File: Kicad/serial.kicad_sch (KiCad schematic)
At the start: 9 parts, among them J801 Conn_02x05, J802 DB9_Male_MountingHoles, U801 ST3232CDR

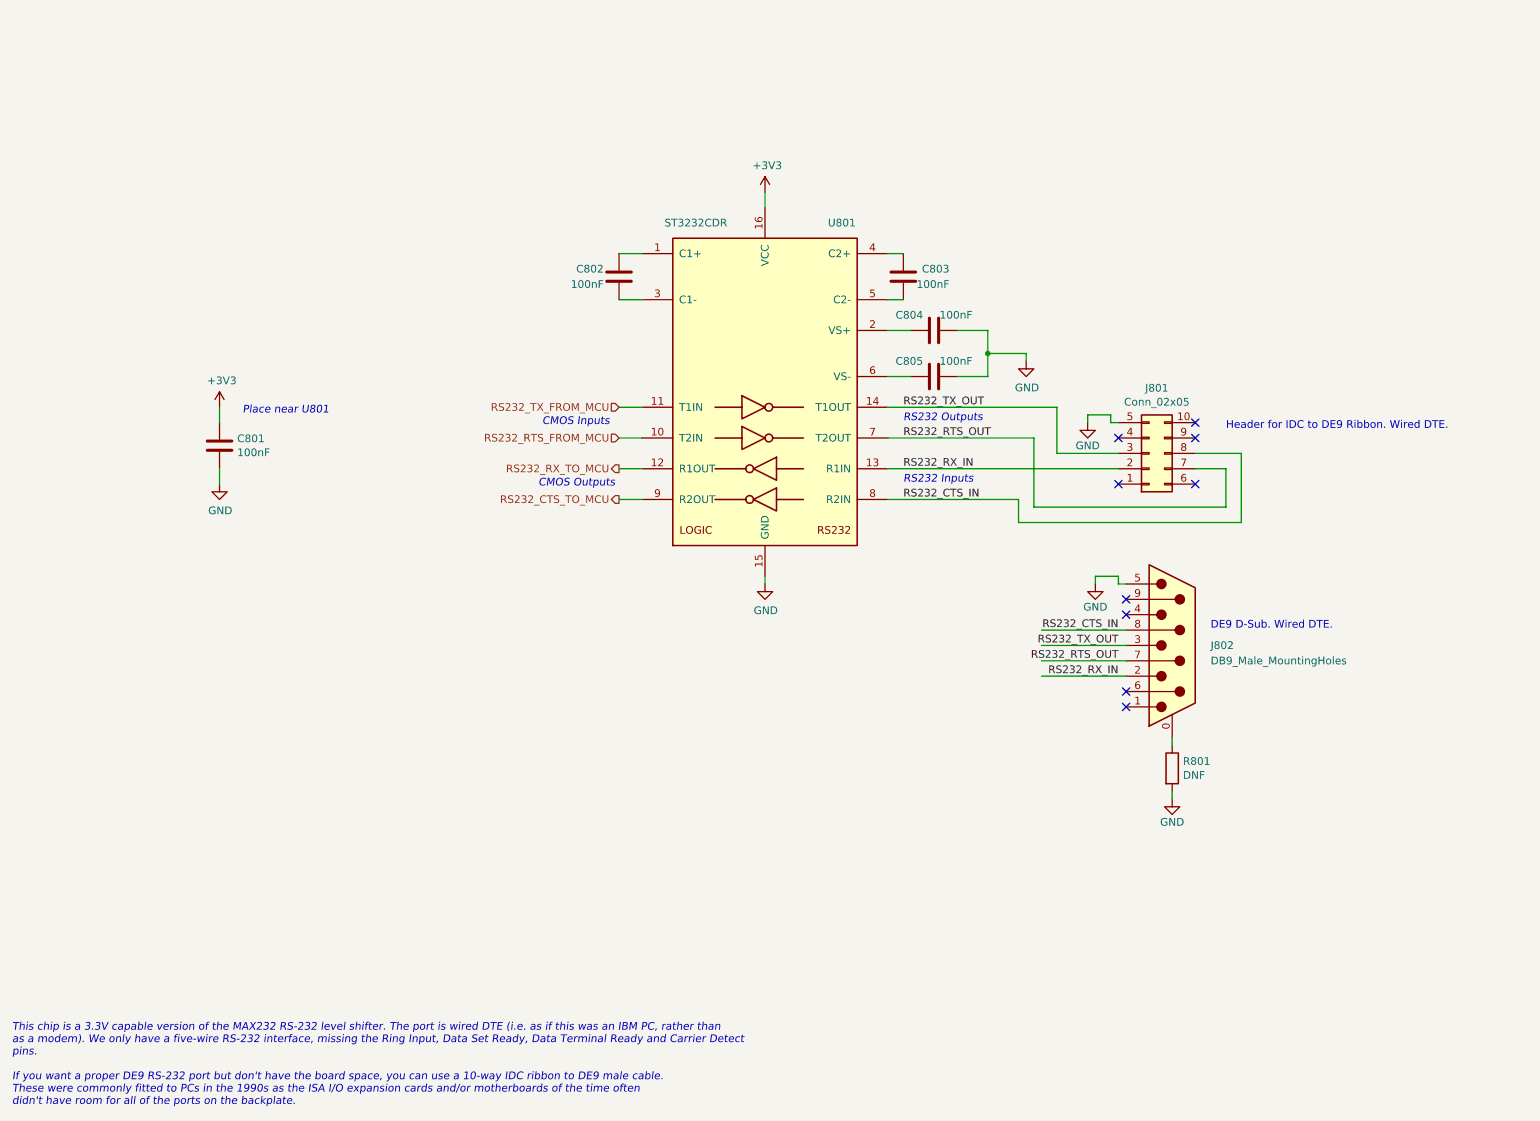
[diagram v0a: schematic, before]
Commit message: Update schematic files to Kicad 6.
Had to fix some symbols which didn't have perfect matches in K6.
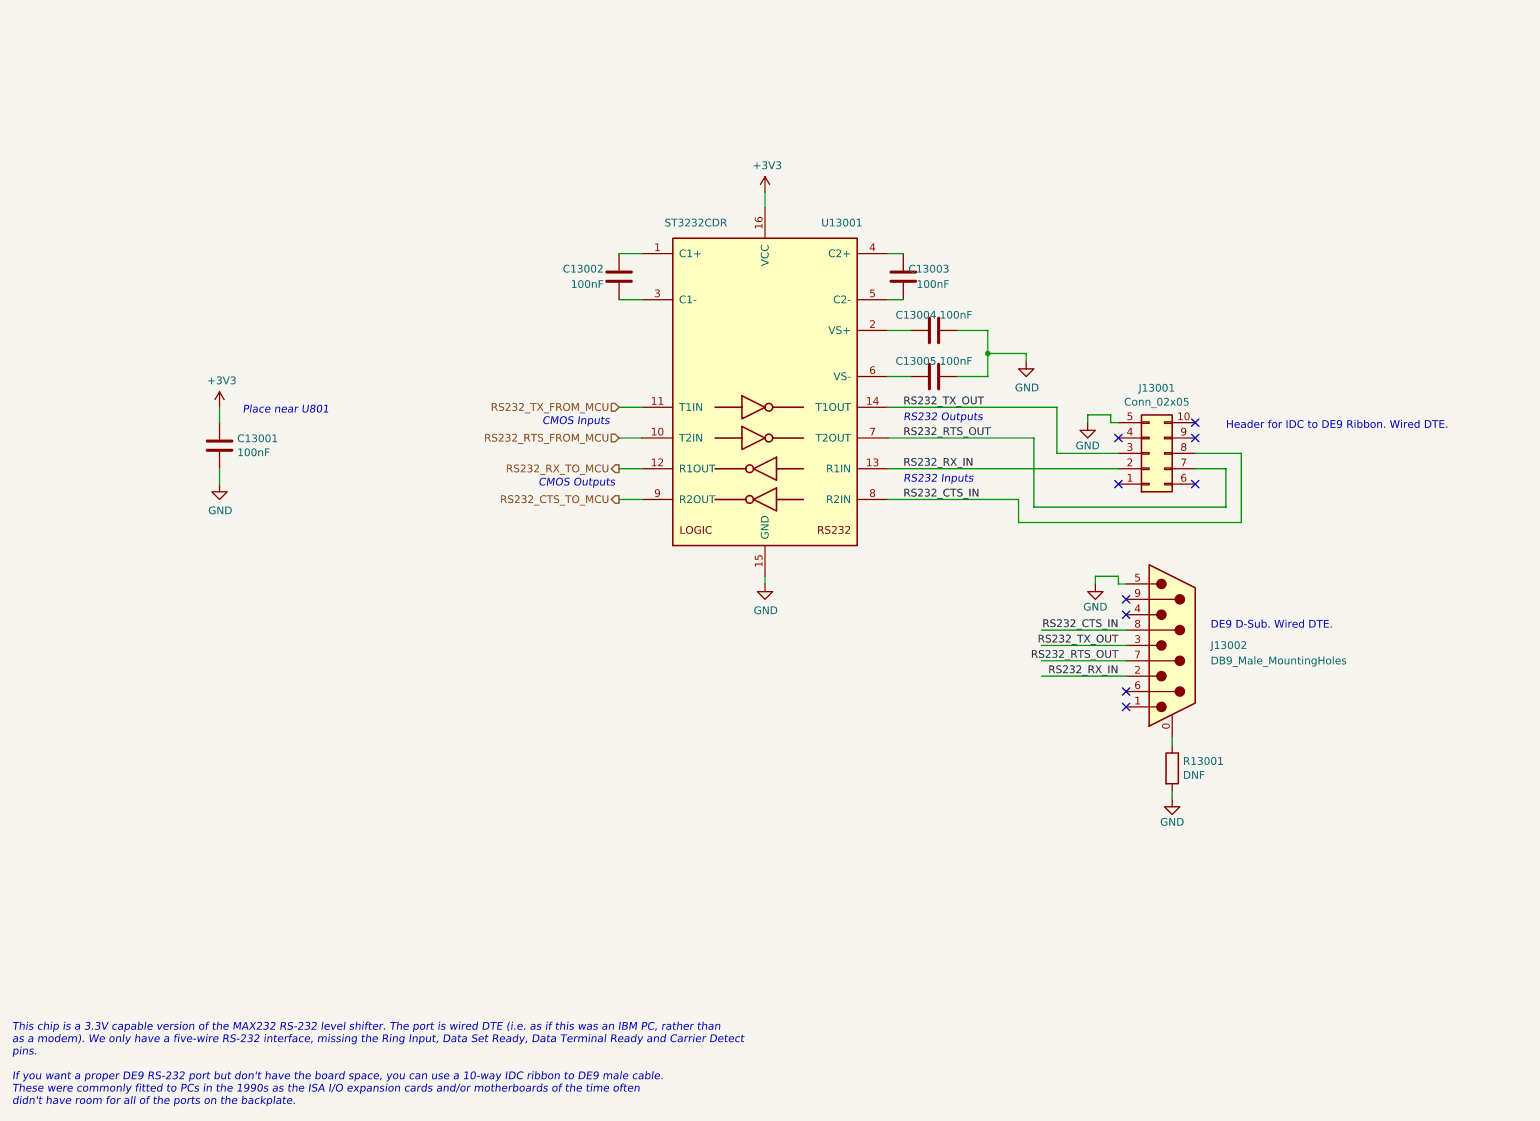
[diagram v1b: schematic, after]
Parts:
- renumbered C801 to C13001, C802 to C13002, C803 to C13003, C804 to C13004, C805 to C13005, J801 to J13001, J802 to J13002, R801 to R13001, U801 to U13001
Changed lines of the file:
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@@
   (symbol (lib_id "Connector_Generic:Conn_02x05_Top_Bottom") (at 201.93 87.63 0) (mirror x) (unit 1)
     (in_bom yes) (on_board yes)
-    (property "Reference" "J801" (id 0) (at 203.2 76.835 0))
+    (property "Reference" "J13001" (id 0) (at 203.2 76.835 0))
     (property "Value" "Conn_02x05" (id 1) (at 203.2 79.1464 0))
     (property "Footprint" "Connector_IDC:IDC-Header_2x05_P2.54mm_Vertical" (id 2) (at 201.93 87.63 0)
@@
   (symbol (lib_id "power:GND") (at 191.77 82.55 0) (unit 1)
     (in_bom yes) (on_board yes)
-    (property "Reference" "#PWR0806" (id 0) (at 191.77 88.9 0)
+    (property "Reference" "#PWR013006" (id 0) (at 191.77 88.9 0)
       (effects (font (size 1.27 1.27)) hide)
     )
@@
   (symbol (lib_id "Interface_UART:MAX232") (at 138.43 77.47 0) (unit 1)
     (in_bom yes) (on_board yes)
-    (property "Reference" "U801" (id 0) (at 151.13 49.53 0))
+    (property "Reference" "U13001" (id 0) (at 151.13 49.53 0))
     (property "Value" "ST3232CDR" (id 1) (at 127 49.53 0))
     (property "Footprint" "Package_SO:SO-16_5.3x10.2mm_P1.27mm" (id 2) (at 139.7 104.14 0)
@@
   (symbol (lib_id "power:GND") (at 181.61 72.39 0) (unit 1)
     (in_bom yes) (on_board yes)
-    (property "Reference" "#PWR0805" (id 0) (at 181.61 78.74 0)
+    (property "Reference" "#PWR013005" (id 0) (at 181.61 78.74 0)
       (effects (font (size 1.27 1.27)) hide)
     )
@@
   (symbol (lib_id "Device:C") (at 161.29 58.42 0) (unit 1)
     (in_bom yes) (on_board yes)
-    (property "Reference" "C803" (id 0) (at 168.91 57.15 0)
+    (property "Reference" "C13003" (id 0) (at 168.91 57.15 0)
       (effects (font (size 1.27 1.27)) (justify right))
     )
@@
   (symbol (lib_id "Device:C") (at 166.37 74.93 270) (unit 1)
     (in_bom yes) (on_board yes)
-    (property "Reference" "C805" (id 0) (at 160.02 72.39 90)
+    (property "Reference" "C13005" (id 0) (at 160.02 72.39 90)
       (effects (font (size 1.27 1.27)) (justify left))
     )
@@
   (symbol (lib_id "Device:C") (at 114.3 58.42 180) (unit 1)
     (in_bom yes) (on_board yes)
-    (property "Reference" "C802" (id 0) (at 111.76 57.15 0)
+    (property "Reference" "C13002" (id 0) (at 111.76 57.15 0)
       (effects (font (size 1.27 1.27)) (justify left))
     )
@@
   (symbol (lib_id "Device:C") (at 48.26 86.36 180) (unit 1)
     (in_bom yes) (on_board yes)
-    (property "Reference" "C801" (id 0) (at 51.181 85.1916 0)
+    (property "Reference" "C13001" (id 0) (at 51.181 85.1916 0)
       (effects (font (size 1.27 1.27)) (justify right))
     )
@@
   (symbol (lib_id "power:+3V3") (at 138.43 44.45 0) (unit 1)
     (in_bom yes) (on_board yes)
-    (property "Reference" "#PWR0803" (id 0) (at 138.43 48.26 0)
+    (property "Reference" "#PWR013003" (id 0) (at 138.43 48.26 0)
       (effects (font (size 1.27 1.27)) hide)
     )
@@
   (symbol (lib_id "power:+3V3") (at 48.26 80.01 0) (unit 1)
     (in_bom yes) (on_board yes)
-    (property "Reference" "#PWR0801" (id 0) (at 48.26 83.82 0)
+    (property "Reference" "#PWR013001" (id 0) (at 48.26 83.82 0)
       (effects (font (size 1.27 1.27)) hide)
     )
@@
   (symbol (lib_id "power:GND") (at 48.26 92.71 0) (unit 1)
     (in_bom yes) (on_board yes)
-    (property "Reference" "#PWR0802" (id 0) (at 48.26 99.06 0)
+    (property "Reference" "#PWR013002" (id 0) (at 48.26 99.06 0)
       (effects (font (size 1.27 1.27)) hide)
     )
@@
   (symbol (lib_id "Device:C") (at 166.37 67.31 270) (unit 1)
     (in_bom yes) (on_board yes)
-    (property "Reference" "C804" (id 0) (at 160.02 64.77 90)
+    (property "Reference" "C13004" (id 0) (at 160.02 64.77 90)
       (effects (font (size 1.27 1.27)) (justify left))
     )
@@
   (symbol (lib_id "power:GND") (at 138.43 109.22 0) (unit 1)
     (in_bom yes) (on_board yes)
-    (property "Reference" "#PWR0804" (id 0) (at 138.43 115.57 0)
+    (property "Reference" "#PWR013004" (id 0) (at 138.43 115.57 0)
       (effects (font (size 1.27 1.27)) hide)
     )
@@
   (symbol (lib_id "Connector:DB9_Male_MountingHoles") (at 205.74 119.38 0) (unit 1)
     (in_bom yes) (on_board yes)
-    (property "Reference" "J802" (id 0) (at 212.09 119.38 0)
+    (property "Reference" "J13002" (id 0) (at 212.09 119.38 0)
       (effects (font (size 1.27 1.27)) (justify left))
     )
@@
   (symbol (lib_id "power:GND") (at 193.04 109.22 0) (unit 1)
     (in_bom yes) (on_board yes)
-    (property "Reference" "#PWR0807" (id 0) (at 193.04 115.57 0)
+    (property "Reference" "#PWR013007" (id 0) (at 193.04 115.57 0)
       (effects (font (size 1.27 1.27)) hide)
     )
@@
   (symbol (lib_id "power:GND") (at 205.74 144.78 0) (unit 1)
     (in_bom yes) (on_board yes)
-    (property "Reference" "#PWR0808" (id 0) (at 205.74 151.13 0)
+    (property "Reference" "#PWR013008" (id 0) (at 205.74 151.13 0)
       (effects (font (size 1.27 1.27)) hide)
     )
@@
   (symbol (lib_id "Device:R") (at 205.74 139.7 0) (unit 1)
     (in_bom yes) (on_board yes)
-    (property "Reference" "R801" (id 0) (at 207.518 138.5316 0)
-      (effects (font (size 1.27 1.27)) (justify left))
-    )
+    (property "Reference" "R13001" (id 0) (at 207.518 138.5316 0)
+      (effects (font (size 1.27 1.27)) (justify left))
+    )

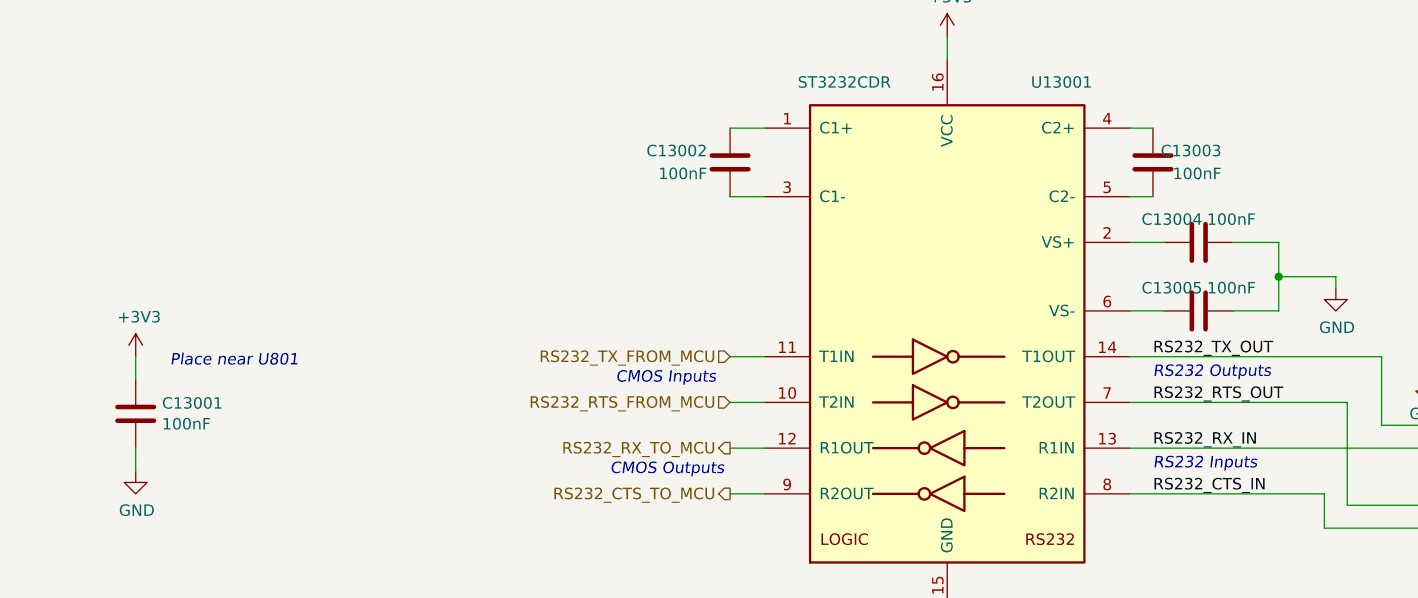
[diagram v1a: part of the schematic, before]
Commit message: Set missing footprints and update PCB
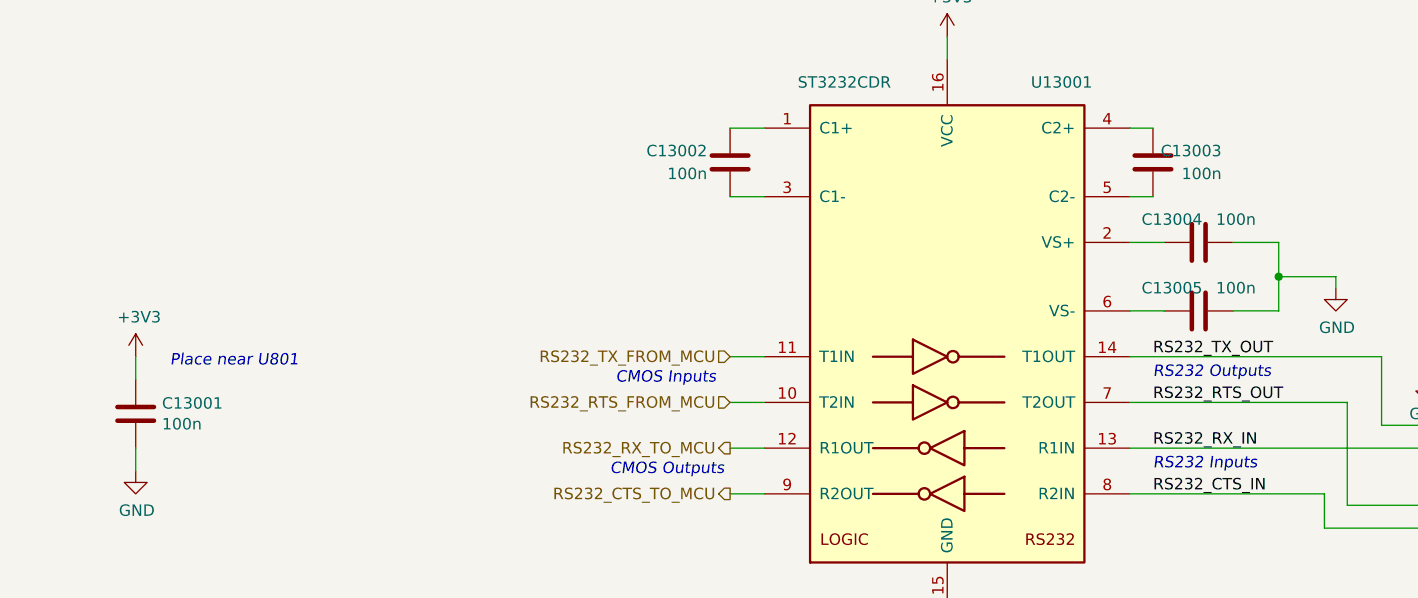
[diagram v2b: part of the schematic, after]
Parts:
- C13001, C13002, C13003, C13004, C13005: value 100nF -> 100n; Digikey BC1150CT-ND -> (none); JLCPCB Collection (none) -> Basic; LCSC Part# (none) -> C49678; MPN CPL-CAP-X7R-0805-100NF-50V -> CC0805KRX7R9BB104
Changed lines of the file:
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@@
       (effects (font (size 1.27 1.27)) (justify right))
     )
-    (property "Value" "100nF" (id 1) (at 168.91 59.69 0)
+    (property "Value" "100n" (id 1) (at 168.91 59.69 0)
       (effects (font (size 1.27 1.27)) (justify right))
     )
@@
       (effects (font (size 1.27 1.27)) hide)
     )
-    (property "Digikey" "BC1150CT-ND" (id 6) (at 161.29 58.42 0)
-      (effects (font (size 1.27 1.27)) hide)
-    )
-    (property "MPN" "CPL-CAP-X7R-0805-100NF-50V" (id 7) (at 161.29 58.42 0)
+    (property "Digikey" "~" (id 6) (at 161.29 58.42 0)
+      (effects (font (size 1.27 1.27)) hide)
+    )
+    (property "MPN" "CC0805KRX7R9BB104" (id 7) (at 161.29 58.42 0)
       (effects (font (size 1.27 1.27)) hide)
     )
@@
       (effects (font (size 1.27 1.27)) hide)
     )
+    (property "JLCPCB Collection" "Basic" (id 11) (at 161.29 58.42 0)
+      (effects (font (size 1.27 1.27)) hide)
+    )
+    (property "LCSC Part#" "C49678" (id 12) (at 161.29 58.42 0)
+      (effects (font (size 1.27 1.27)) hide)
+    )
     (pin "1")
     (pin "2")
@@
       (effects (font (size 1.27 1.27)) (justify left))
     )
-    (property "Value" "100nF" (id 1) (at 172.72 72.39 90)
+    (property "Value" "100n" (id 1) (at 172.72 72.39 90)
       (effects (font (size 1.27 1.27)) (justify right))
     )
@@
       (effects (font (size 1.27 1.27)) hide)
     )
-    (property "Digikey" "BC1150CT-ND" (id 6) (at 166.37 74.93 0)
-      (effects (font (size 1.27 1.27)) hide)
-    )
-    (property "MPN" "CPL-CAP-X7R-0805-100NF-50V" (id 7) (at 166.37 74.93 0)
+    (property "Digikey" "~" (id 6) (at 166.37 74.93 0)
+      (effects (font (size 1.27 1.27)) hide)
+    )
+    (property "MPN" "CC0805KRX7R9BB104" (id 7) (at 166.37 74.93 0)
       (effects (font (size 1.27 1.27)) hide)
     )
@@
       (effects (font (size 1.27 1.27)) hide)
     )
+    (property "JLCPCB Collection" "Basic" (id 11) (at 166.37 74.93 0)
+      (effects (font (size 1.27 1.27)) hide)
+    )
+    (property "LCSC Part#" "C49678" (id 12) (at 166.37 74.93 0)
+      (effects (font (size 1.27 1.27)) hide)
+    )
     (pin "1")
     (pin "2")
@@
       (effects (font (size 1.27 1.27)) (justify left))
     )
-    (property "Value" "100nF" (id 1) (at 111.76 59.69 0)
+    (property "Value" "100n" (id 1) (at 111.76 59.69 0)
       (effects (font (size 1.27 1.27)) (justify left))
     )
@@
       (effects (font (size 1.27 1.27)) hide)
     )
-    (property "Digikey" "BC1150CT-ND" (id 6) (at 114.3 58.42 0)
-      (effects (font (size 1.27 1.27)) hide)
-    )
-    (property "MPN" "CPL-CAP-X7R-0805-100NF-50V" (id 7) (at 114.3 58.42 0)
+    (property "Digikey" "~" (id 6) (at 114.3 58.42 0)
+      (effects (font (size 1.27 1.27)) hide)
+    )
+    (property "MPN" "CC0805KRX7R9BB104" (id 7) (at 114.3 58.42 0)
       (effects (font (size 1.27 1.27)) hide)
     )
@@
       (effects (font (size 1.27 1.27)) hide)
     )
+    (property "JLCPCB Collection" "Basic" (id 11) (at 114.3 58.42 0)
+      (effects (font (size 1.27 1.27)) hide)
+    )
+    (property "LCSC Part#" "C49678" (id 12) (at 114.3 58.42 0)
+      (effects (font (size 1.27 1.27)) hide)
+    )
     (pin "1")
     (pin "2")
@@
       (effects (font (size 1.27 1.27)) (justify right))
     )
-    (property "Value" "100nF" (id 1) (at 51.181 87.503 0)
+    (property "Value" "100n" (id 1) (at 51.181 87.503 0)
       (effects (font (size 1.27 1.27)) (justify right))
     )
@@
       (effects (font (size 1.27 1.27)) hide)
     )
-    (property "Digikey" "BC1150CT-ND" (id 6) (at 48.26 86.36 0)
-      (effects (font (size 1.27 1.27)) hide)
-    )
-    (property "MPN" "CPL-CAP-X7R-0805-100NF-50V" (id 7) (at 48.26 86.36 0)
+    (property "Digikey" "~" (id 6) (at 48.26 86.36 0)
+      (effects (font (size 1.27 1.27)) hide)
+    )
+    (property "MPN" "CC0805KRX7R9BB104" (id 7) (at 48.26 86.36 0)
       (effects (font (size 1.27 1.27)) hide)
     )
@@
     )
     (property "Voltage" "10V" (id 10) (at 48.26 86.36 0)
+      (effects (font (size 1.27 1.27)) hide)
+    )
+    (property "JLCPCB Collection" "Basic" (id 11) (at 48.26 86.36 0)
+      (effects (font (size 1.27 1.27)) hide)
+    )
+    (property "LCSC Part#" "C49678" (id 12) (at 48.26 86.36 0)
       (effects (font (size 1.27 1.27)) hide)
     )
@@
       (effects (font (size 1.27 1.27)) (justify left))
     )
-    (property "Value" "100nF" (id 1) (at 172.72 64.77 90)
+    (property "Value" "100n" (id 1) (at 172.72 64.77 90)
       (effects (font (size 1.27 1.27)) (justify right))
     )
@@
       (effects (font (size 1.27 1.27)) hide)
     )
-    (property "Digikey" "BC1150CT-ND" (id 6) (at 166.37 67.31 0)
-      (effects (font (size 1.27 1.27)) hide)
-    )
-    (property "MPN" "CPL-CAP-X7R-0805-100NF-50V" (id 7) (at 166.37 67.31 0)
+    (property "Digikey" "~" (id 6) (at 166.37 67.31 0)
+      (effects (font (size 1.27 1.27)) hide)
+    )
+    (property "MPN" "CC0805KRX7R9BB104" (id 7) (at 166.37 67.31 0)
       (effects (font (size 1.27 1.27)) hide)
     )
@@
       (effects (font (size 1.27 1.27)) hide)
     )
+    (property "JLCPCB Collection" "Basic" (id 11) (at 166.37 67.31 0)
+      (effects (font (size 1.27 1.27)) hide)
+    )
+    (property "LCSC Part#" "C49678" (id 12) (at 166.37 67.31 0)
+      (effects (font (size 1.27 1.27)) hide)
+    )
